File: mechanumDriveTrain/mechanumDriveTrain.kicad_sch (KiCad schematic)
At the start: 39 parts, among them IC1 TCAN3414DR, J1 XT30U-M, J2 BM02B-SRSS-TB, J3 5 pin dupont, J4 5 pin dupont, U1 Teensy 4.1, U2 LD1117S50TR_SOT223

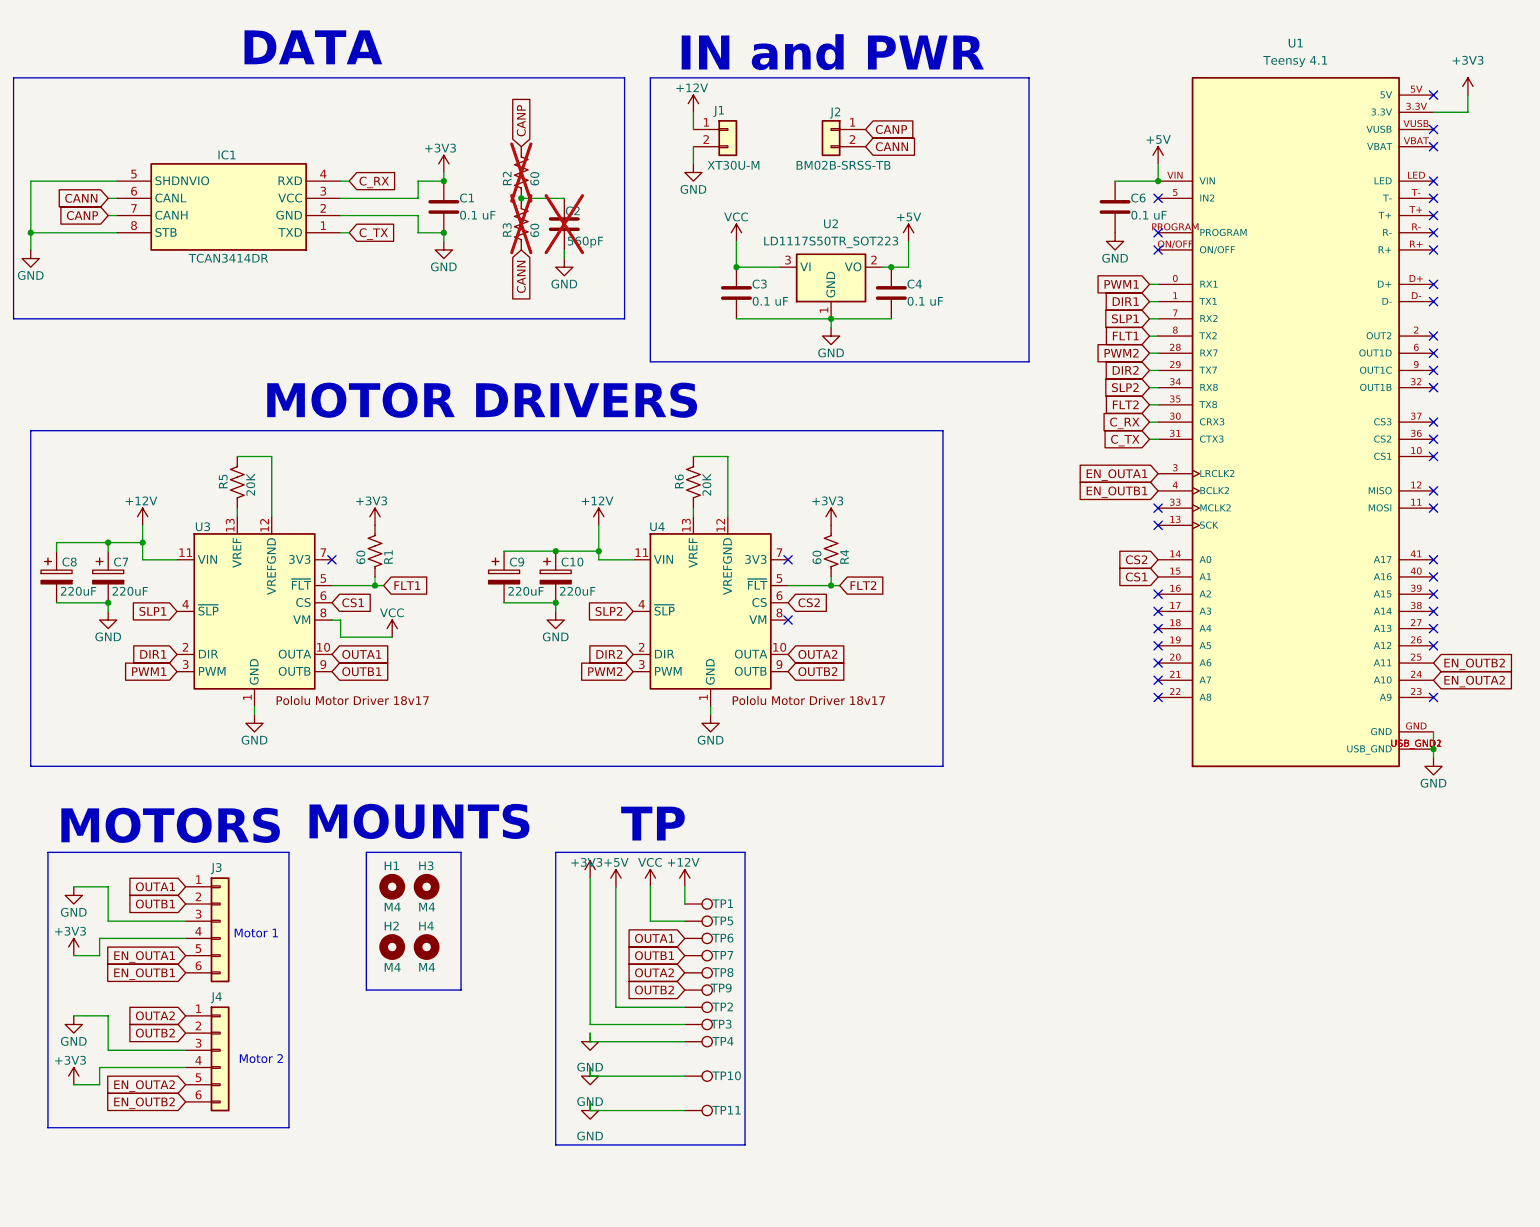
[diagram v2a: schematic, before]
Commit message: Updated routing, added labels
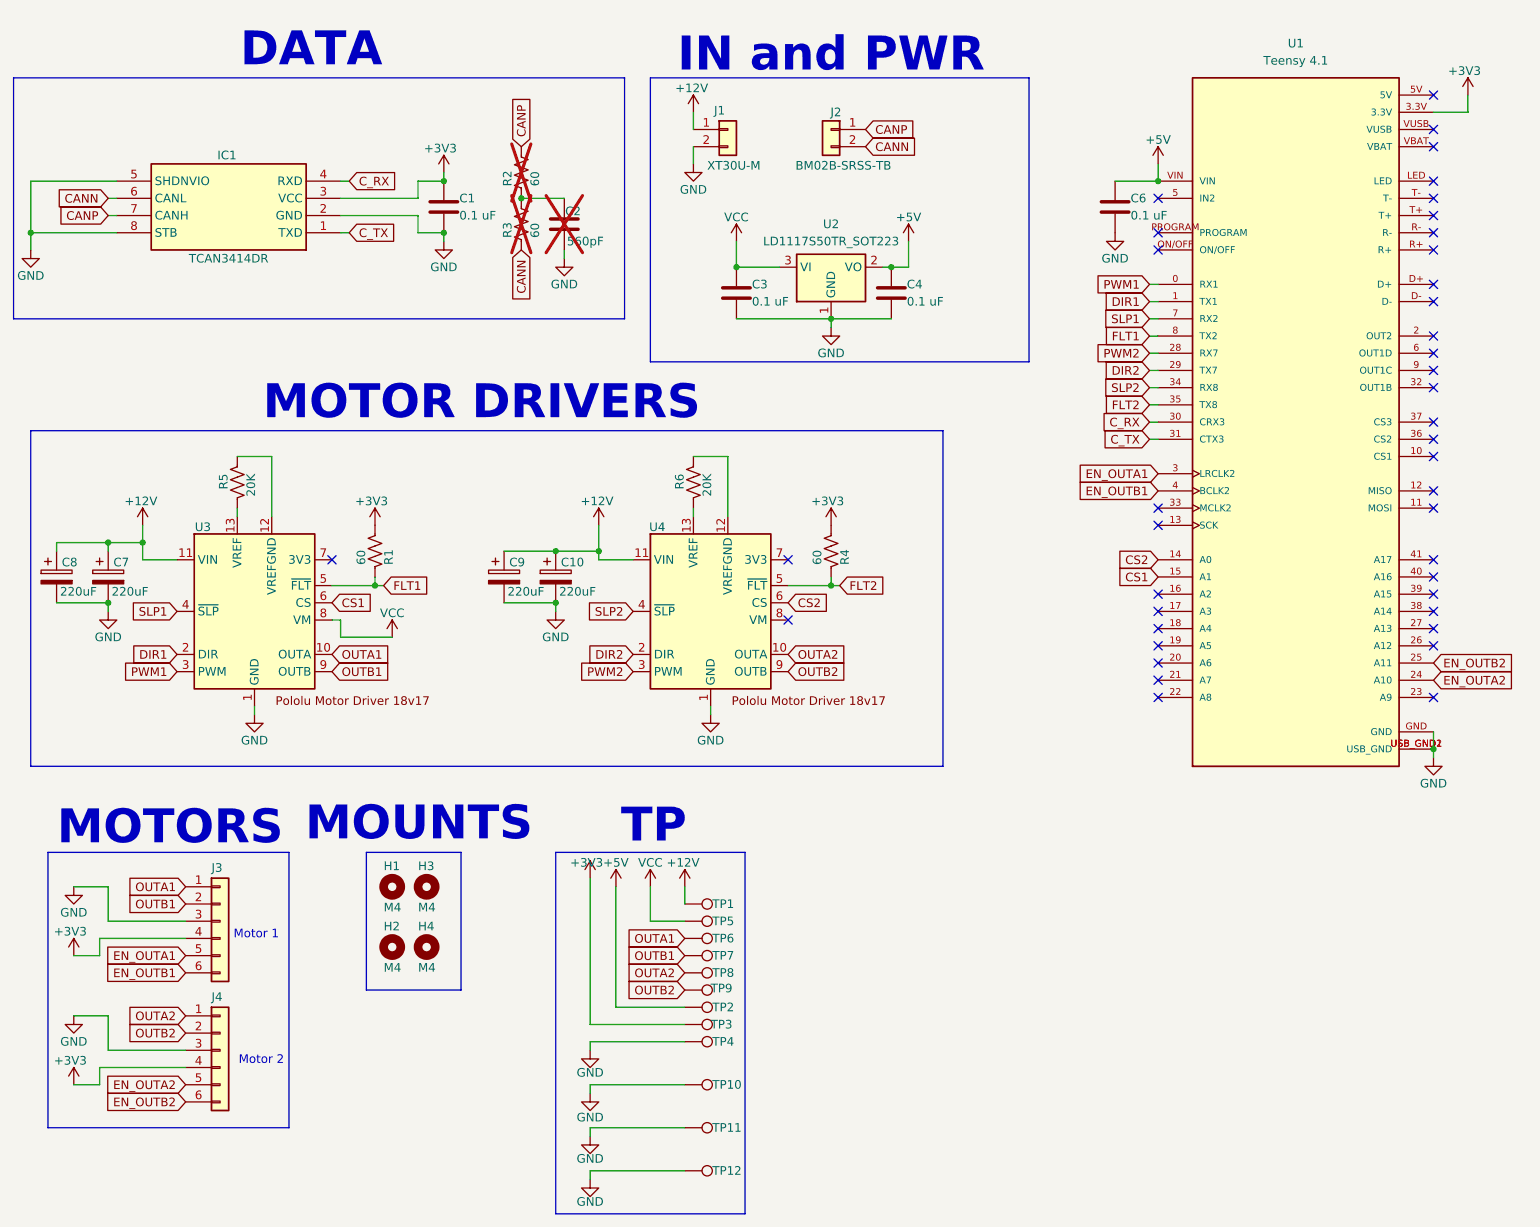
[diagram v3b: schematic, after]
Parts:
- added TP12: ~, TestPoint:TestPoint_Loop_D1.80mm_Drill1.0mm_Beaded, symbol Connector:TestPoint
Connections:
- net GND: now also TP12.1
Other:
- moved on the sheet: TP10, TP11
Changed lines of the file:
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@@
 	(wire
 		(pts
+			(xy 100.33 182.88) (xy 100.33 184.15)
+		)
+		(stroke
+			(width 0)
+			(type default)
+		)
+	)
+	(wire
+		(pts
 			(xy 177.8 36.83) (xy 184.15 36.83)
 		)
@@
 	(wire
 		(pts
-			(xy 100.33 168.91) (xy 100.33 167.64)
+			(xy 100.33 170.18) (xy 100.33 171.45)
 		)
 		(stroke
@@
 	(wire
 		(pts
-			(xy 100.33 173.99) (xy 114.3 173.99)
+			(xy 100.33 176.53) (xy 114.3 176.53)
 		)
 		(stroke
@@
 	(wire
 		(pts
-			(xy 100.33 163.83) (xy 100.33 162.56)
+			(xy 100.33 163.83) (xy 100.33 165.1)
 		)
 		(stroke
@@
 	(wire
 		(pts
-			(xy 100.33 173.99) (xy 100.33 172.72)
+			(xy 100.33 176.53) (xy 100.33 177.8)
 		)
 		(stroke
@@
 	(wire
 		(pts
-			(xy 100.33 168.91) (xy 114.3 168.91)
+			(xy 100.33 170.18) (xy 114.3 170.18)
 		)
 		(stroke
@@
 	(wire
 		(pts
+			(xy 100.33 182.88) (xy 114.3 182.88)
+		)
+		(stroke
+			(width 0)
+			(type default)
+		)
+	)
+	(wire
+		(pts
 			(xy 135.89 58.42) (xy 135.89 57.15)
 		)
@@
 	(rectangle
 		(start 95.25 135.89)
-		(end 123.19 179.07)
+		(end 123.19 189.23)
 		(stroke
 			(width 0)
@@
 		(on_board yes)
 		(dnp no)
-		(fields_autoplaced yes)
 		(property "Reference" "#PWR028"
 			(at 229.87 27.94 0)
@@
 		)
 		(property "Value" "+3V3"
-			(at 229.87 19.05 0)
+			(at 229.362 20.574 0)
 			(effects
 				(font
@@
 	(symbol
 		(lib_id "Connector:TestPoint")
-		(at 114.3 168.91 270)
+		(at 114.3 170.18 270)
 		(unit 1)
 		(exclude_from_sim no)
@@
 		(dnp no)
 		(property "Reference" "TP10"
-			(at 118.3641 168.91 90)
+			(at 118.3641 170.18 90)
 			(effects
 				(font
@@
 		)
 		(property "Value" "~"
-			(at 116.3321 171.45 0)
+			(at 116.3321 172.72 0)
 			(effects
 				(font
@@
 		)
 		(property "Footprint" "TestPoint:TestPoint_Loop_D1.80mm_Drill1.0mm_Beaded"
-			(at 114.3 173.99 0)
+			(at 114.3 175.26 0)
 			(effects
 				(font
@@
 		)
 		(property "Datasheet" "~"
-			(at 114.3 173.99 0)
+			(at 114.3 175.26 0)
 			(effects
 				(font
@@
 		)
 		(property "Description" "test point"
-			(at 114.3 168.91 0)
+			(at 114.3 170.18 0)
 			(effects
 				(font
@@
 	)
 	(symbol
+		(lib_id "Connector:TestPoint")
+		(at 114.3 182.88 270)
+		(unit 1)
+		(exclude_from_sim no)
+		(in_bom yes)
+		(on_board yes)
+		(dnp no)
+		(property "Reference" "TP12"
+			(at 118.3641 182.88 90)
+			(effects
+				(font
+					(size 1.27 1.27)
+				)
+				(justify left)
+			)
+		)
+		(property "Value" "~"
+			(at 116.3321 185.42 0)
+			(effects
+				(font
+					(size 1.27 1.27)
+				)
+				(justify left)
+			)
+		)
+		(property "Footprint" "TestPoint:TestPoint_Loop_D1.80mm_Drill1.0mm_Beaded"
+			(at 114.3 187.96 0)
+			(effects
+				(font
+					(size 1.27 1.27)
+				)
+				(hide yes)
+			)
+		)
+		(property "Datasheet" "~"
+			(at 114.3 187.96 0)
+			(effects
+				(font
+					(size 1.27 1.27)
+				)
+				(hide yes)
+			)
+		)
+		(property "Description" "test point"
+			(at 114.3 182.88 0)
+			(effects
+				(font
+					(size 1.27 1.27)
+				)
+				(hide yes)
+			)
+		)
+		(pin "1"
+		)
+		(instances
+			(project "mechanumDriveTrain"
+				(path "/150d9912-2987-4a4a-be7d-95dc51376246"
+					(reference "TP12")
+					(unit 1)
+				)
+			)
+		)
+	)
+	(symbol
 		(lib_id "power:GND")
 		(at 17.78 46.99 0)
@@
 	(symbol
 		(lib_id "power:GND")
+		(at 100.33 184.15 0)
+		(unit 1)
+		(exclude_from_sim no)
+		(in_bom yes)
+		(on_board yes)
+		(dnp no)
+		(property "Reference" "#PWR034"
+			(at 100.33 190.5 0)
+			(effects
+				(font
+					(size 1.27 1.27)
+				)
+				(hide yes)
+			)
+		)
+		(property "Value" "GND"
+			(at 100.33 187.452 0)
+			(effects
+				(font
+					(size 1.27 1.27)
+				)
+			)
+		)
+		(property "Footprint" ""
+			(at 100.33 184.15 0)
+			(effects
+				(font
+					(size 1.27 1.27)
+				)
+				(hide yes)
+			)
+		)
+		(property "Datasheet" ""
+			(at 100.33 184.15 0)
+			(effects
+				(font
+					(size 1.27 1.27)
+				)
+				(hide yes)
+			)
+		)
+		(property "Description" "Power symbol creates a global label with name \"GND\" , ground"
+			(at 100.33 184.15 0)
+			(effects
+				(font
+					(size 1.27 1.27)
+				)
+				(hide yes)
+			)
+		)
+		(pin "1"
+		)
+		(instances
+			(project "mechanumDriveTrain"
+				(path "/150d9912-2987-4a4a-be7d-95dc51376246"
+					(reference "#PWR034")
+					(unit 1)
+				)
+			)
+		)
+	)
+	(symbol
+		(lib_id "power:GND")
 		(at 78.74 45.72 0)
 		(unit 1)
@@
 	(symbol
 		(lib_id "power:GND")
-		(at 100.33 162.56 0)
+		(at 100.33 165.1 0)
 		(unit 1)
 		(exclude_from_sim no)
@@
 		(dnp no)
 		(property "Reference" "#PWR026"
-			(at 100.33 168.91 0)
+			(at 100.33 171.45 0)
 			(effects
 				(font
@@
 		)
 		(property "Value" "GND"
-			(at 100.33 167.64 0)
+			(at 100.33 168.402 0)
 			(effects
 				(font
@@
 		)
 		(property "Footprint" ""
-			(at 100.33 162.56 0)
+			(at 100.33 165.1 0)
 			(effects
 				(font
@@
 		)
 		(property "Datasheet" ""
-			(at 100.33 162.56 0)
+			(at 100.33 165.1 0)
 			(effects
 				(font
@@
 		)
 		(property "Description" "Power symbol creates a global label with name \"GND\" , ground"
-			(at 100.33 162.56 0)
+			(at 100.33 165.1 0)
 			(effects
 				(font
@@
 	(symbol
 		(lib_id "power:GND")
-		(at 100.33 167.64 0)
+		(at 100.33 171.45 0)
 		(unit 1)
 		(exclude_from_sim no)
@@
 		(dnp no)
 		(property "Reference" "#PWR032"
-			(at 100.33 173.99 0)
+			(at 100.33 177.8 0)
 			(effects
 				(font
@@
 		)
 		(property "Value" "GND"
-			(at 100.33 172.72 0)
+			(at 100.33 175.006 0)
 			(effects
 				(font
@@
 		)
 		(property "Footprint" ""
-			(at 100.33 167.64 0)
+			(at 100.33 171.45 0)
 			(effects
 				(font
@@
 		)
 		(property "Datasheet" ""
-			(at 100.33 167.64 0)
+			(at 100.33 171.45 0)
 			(effects
 				(font
@@
 		)
 		(property "Description" "Power symbol creates a global label with name \"GND\" , ground"
-			(at 100.33 167.64 0)
+			(at 100.33 171.45 0)
 			(effects
 				(font
@@
 	(symbol
 		(lib_id "power:GND")
-		(at 100.33 172.72 0)
+		(at 100.33 177.8 0)
 		(unit 1)
 		(exclude_from_sim no)
@@
 		(dnp no)
 		(property "Reference" "#PWR033"
-			(at 100.33 179.07 0)
+			(at 100.33 184.15 0)
 			(effects
 				(font
@@
 		)
 		(property "Value" "GND"
-			(at 100.33 177.8 0)
+			(at 100.33 181.102 0)
 			(effects
 				(font
@@
 		)
 		(property "Footprint" ""
-			(at 100.33 172.72 0)
+			(at 100.33 177.8 0)
 			(effects
 				(font
@@
 		)
 		(property "Datasheet" ""
-			(at 100.33 172.72 0)
+			(at 100.33 177.8 0)
 			(effects
 				(font
@@
 		)
 		(property "Description" "Power symbol creates a global label with name \"GND\" , ground"
-			(at 100.33 172.72 0)
+			(at 100.33 177.8 0)
 			(effects
 				(font
@@
 	(symbol
 		(lib_id "Connector:TestPoint")
-		(at 114.3 173.99 270)
+		(at 114.3 176.53 270)
 		(unit 1)
 		(exclude_from_sim no)
@@
 		(dnp no)
 		(property "Reference" "TP11"
-			(at 118.3641 173.99 90)
+			(at 118.3641 176.53 90)
 			(effects
 				(font
@@
 		)
 		(property "Value" "~"
-			(at 116.3321 176.53 0)
+			(at 116.3321 179.07 0)
 			(effects
 				(font
@@
 		)
 		(property "Footprint" "TestPoint:TestPoint_Loop_D1.80mm_Drill1.0mm_Beaded"
-			(at 114.3 179.07 0)
+			(at 114.3 181.61 0)
 			(effects
 				(font
@@
 		)
 		(property "Datasheet" "~"
-			(at 114.3 179.07 0)
+			(at 114.3 181.61 0)
 			(effects
 				(font
@@
 		)
 		(property "Description" "test point"
-			(at 114.3 173.99 0)
+			(at 114.3 176.53 0)
 			(effects
 				(font

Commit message: Updated routing, created images, created gerbers
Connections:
- net CS1: now also U1.23 (A9); no longer U1.15 (A1)
- net CS2: now also U1.40 (A16); no longer U1.14 (A0)
- net EN_OUTA1: now also U1.11 (MOSI); no longer U1.3 (LRCLK2)
- net EN_OUTB1: now also U1.12 (MISO); no longer U1.4 (BCLK2)
- net PWM1: now also U1.2 (OUT2); no longer U1.0 (RX1)

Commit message: fixed pullup
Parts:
- R1, R4: value 60 -> 10K
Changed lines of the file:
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@@
 			)
 		)
-		(property "Value" "60"
+		(property "Value" "10K"
 			(at 66.548 93.4719 90)
 			(effects
@@
 			)
 		)
-		(property "Value" "60"
+		(property "Value" "10K"
 			(at 133.858 93.4719 90)
 			(effects
